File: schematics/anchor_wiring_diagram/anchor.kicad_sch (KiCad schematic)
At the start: 98 parts, among them J2 Screw_Terminal_01x01, J3 Screw_Terminal_01x01, J4 Screw_Terminal_01x01, J5 IEC_60320_C14_Receptacle, M1 Crossflow_Fan, M15 Fan, M16 Fan, M2 Crossflow_Fan, M20 Motor_X0, M21 Motor_Y0, M22 Motor_X1, M23 Motor_Y1, M24 Motor_Z2, M25 Motor_Z1, M26 Motor_Z0, M27 Motor_CPAP_Flap, M28 Motor_E0, M3 Fan_4pin, M4 Fan_4pin, M5 Fan_4pin, M6 Fan_4pin, M7 Fan, M8 Fan, SW1 SW_SPST, SW2 SW_SPST, SW5 SW_DPST, SW6 SW_DPST, SW7 SW_DPST, SW8 SW_DPST, T1 Meanwell UHP-200-5, T2 Meanwell UHP-200-48, T3 Meanwell UHP-200-24, U1 e-CAM20_CU0230, U12 Daylight_On_A_Stick_XXL, U13 Daylight_On_A_Stick_XXL, U16 Daylight_On_A_Stick_XXL, U17 Daylight_On_A_Stick_XXL, U2 OLED_HDMI_USB_Display, U20 Daylight_On_A_Stick_XXL, U21 Daylight_On_A_Stick_XXL, U24 Daylight_On_A_Stick_XXL, U25 Daylight_On_A_Stick_XXL, U26 5160T_Plus, U27 Adafruit_Feather_Relay, U29 Schneider_Electric_DPE25G7, U3 Overhub_7-Port_USB_3.0_MTT_Hub, U30 Crydom_D2440_SPST_SSR-NO, U31 Schneider_Electric_DPE25BL, U32 Neopixel_Strip, U33 Crydom_D2440_SPST_SSR-NO, U34 Schneider_Electric_DPE25BL, U37 Schneider_Electric_DPE25BL, U39 Raspberry_Pi, U4 Beacon_Regulator, U40 Beacon_Eddy_Scanner, U41 ThermEX26, U5 BTT_Octopus_Max_EZ, U6 5160T_Plus, U7 5160T_Plus, U8 5160T_Plus, U9 5160T_Plus

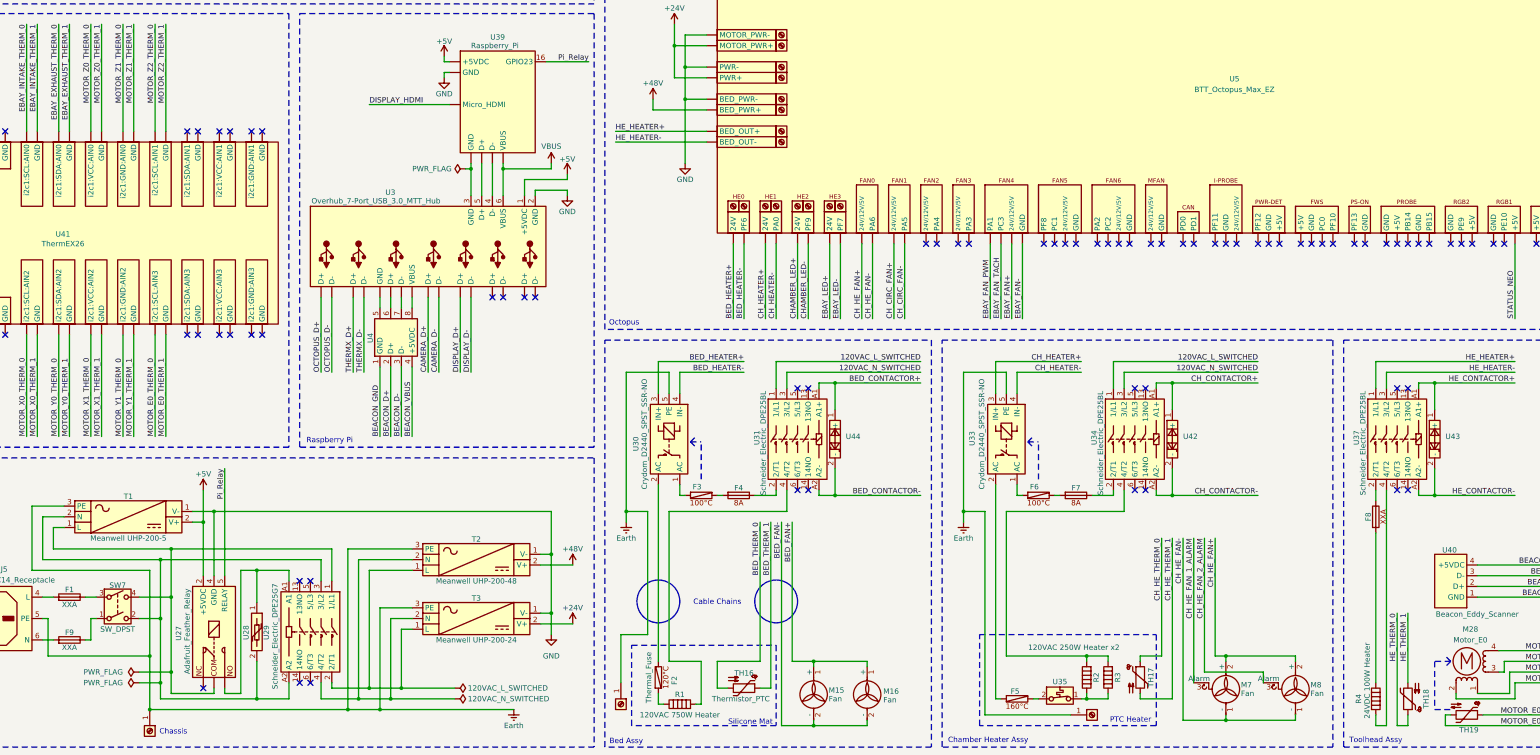
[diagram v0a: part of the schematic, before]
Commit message: schematic: wire up contactors
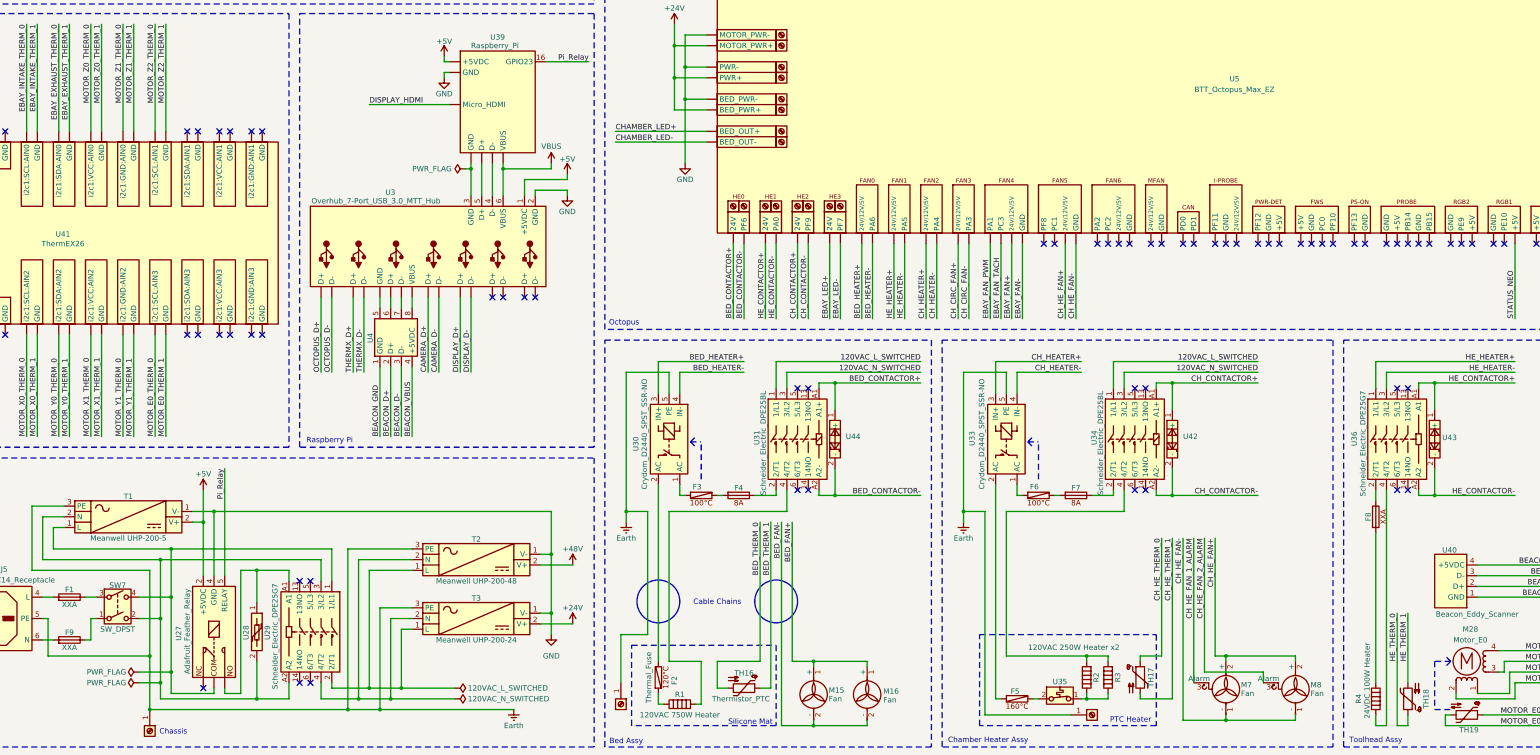
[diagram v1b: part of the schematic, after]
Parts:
- removed U37: Schneider_Electric_DPE25BL, symbol jmatt:Schneider_Electric_DPE25BL
- added U36: Schneider_Electric_DPE25G7, symbol jmatt:Schneider_Electric_DPE25G7
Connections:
- net +48V: no longer U5. (GND)
- net BED_CONTACTOR+: now also U5. (GND)
- net BED_CONTACTOR-: now also U5. (GND)
- net CH_CONTACTOR+: now also U5. (GND)
- net CH_CONTACTOR-: now also U5. (GND)
- net HE_CONTACTOR+: now also U5. (GND), U36.A1
- net HE_CONTACTOR-: now also U5. (GND), U36.A2
- net HE_HEATER+: now also U36.1 (1/L1)
- net HE_HEATER-: now also U36.3 (3/L2)
- net at F8.1: now also U36.2 (2/T1)
- net at U27.: now also U28.1, U29.A1
- net at R4.2: now also U36.4 (4/T2)
- new net: T2.1 (V-), T3.1 (V-), U29.2 (2/T1)
- new net: T2.2 (V+), T3.2 (V+), U29.4 (4/T2)
- no-connect marks 115 -> 109

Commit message: Add frame; k3z
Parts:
- added R5: 220R, symbol Device:R
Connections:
- net STATUS_NEO: now also R5.1; no longer SW8.1
- net at U27.: now also U28.1, U29.A1
- new net: R5.2, SW8.1
- new net: T2.1 (V-), T3.1 (V-), U29.2 (2/T1)
- new net: T2.2 (V+), T3.2 (V+), U29.4 (4/T2)
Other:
- moved on the sheet: SW8, U32
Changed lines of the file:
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@@
 	)
 	(junction
-		(at 64.77 96.52)
+		(at 72.39 96.52)
 		(diameter 0)
 		(color 255 0 0 1)
@@
 	)
 	(no_connect
+		(at 431.8 189.23)
+	)
+	(no_connect
 		(at 284.48 114.3)
 	)
@@
 	)
 	(no_connect
-		(at 100.33 96.52)
+		(at 107.95 96.52)
 	)
 	(no_connect
@@
 	)
 	(no_connect
-		(at 100.33 99.06)
+		(at 107.95 99.06)
 	)
 	(no_connect
@@
 	)
 	(no_connect
-		(at 100.33 101.6)
+		(at 107.95 101.6)
 	)
 	(no_connect
@@
 		(at 365.76 189.23)
 	)
-	(no_connect
-		(at 429.26 189.23)
-	)
 	(polyline
 		(pts
@@
 	(wire
 		(pts
-			(xy 44.45 96.52) (xy 52.07 96.52)
+			(xy 52.07 96.52) (xy 59.69 96.52)
 		)
 		(stroke
@@
 	(wire
 		(pts
+			(xy 429.26 189.23) (xy 429.26 207.01)
+		)
+		(stroke
+			(width 0)
+			(type default)
+		)
+	)
+	(wire
+		(pts
 			(xy 359.41 90.17) (xy 359.41 114.3)
 		)
@@
 	(wire
 		(pts
-			(xy 44.45 95.25) (xy 44.45 96.52)
+			(xy 52.07 95.25) (xy 52.07 96.52)
 		)
 		(stroke
@@
 	(wire
 		(pts
-			(xy 62.23 101.6) (xy 64.77 101.6)
+			(xy 69.85 101.6) (xy 72.39 101.6)
 		)
 		(stroke
@@
 	(wire
 		(pts
+			(xy 57.15 101.6) (xy 59.69 101.6)
+		)
+		(stroke
+			(width 0)
+			(type default)
+		)
+	)
+	(wire
+		(pts
 			(xy 38.1 76.2) (xy 52.07 76.2)
 		)
@@
 	(wire
 		(pts
-			(xy 64.77 99.06) (xy 67.31 99.06)
+			(xy 72.39 99.06) (xy 74.93 99.06)
 		)
 		(stroke
@@
 	(wire
 		(pts
+			(xy 38.1 101.6) (xy 49.53 101.6)
+		)
+		(stroke
+			(width 0)
+			(type default)
+		)
+	)
+	(wire
+		(pts
 			(xy 266.7 222.25) (xy 270.51 222.25)
 		)
@@
 	(wire
 		(pts
-			(xy 62.23 96.52) (xy 64.77 96.52)
+			(xy 69.85 96.52) (xy 72.39 96.52)
 		)
 		(stroke
@@
 	(wire
 		(pts
-			(xy 66.04 101.6) (xy 66.04 102.87)
+			(xy 73.66 101.6) (xy 73.66 102.87)
 		)
 		(stroke
@@
 	(wire
 		(pts
-			(xy 67.31 101.6) (xy 66.04 101.6)
+			(xy 74.93 101.6) (xy 73.66 101.6)
 		)
 		(stroke
@@
 	(wire
 		(pts
-			(xy 64.77 101.6) (xy 64.77 99.06)
+			(xy 72.39 101.6) (xy 72.39 99.06)
 		)
 		(stroke
@@
 	(wire
 		(pts
-			(xy 431.8 189.23) (xy 431.8 207.01)
-		)
-		(stroke
-			(width 0)
-			(type default)
-		)
-	)
-	(wire
-		(pts
 			(xy 354.33 22.86) (xy 356.87 22.86)
 		)
@@
 	(wire
 		(pts
-			(xy 64.77 95.25) (xy 64.77 96.52)
+			(xy 72.39 95.25) (xy 72.39 96.52)
 		)
 		(stroke
@@
 	(wire
 		(pts
-			(xy 64.77 96.52) (xy 67.31 96.52)
+			(xy 72.39 96.52) (xy 74.93 96.52)
 		)
 		(stroke
@@
 	(wire
 		(pts
-			(xy 38.1 101.6) (xy 52.07 101.6)
-		)
-		(stroke
-			(width 0)
-			(type default)
-		)
-	)
-	(wire
-		(pts
 			(xy 392.43 99.06) (xy 392.43 114.3)
 		)
@@
 	)
 	(label "STATUS_NEO"
-		(at 431.8 207.01 90)
+		(at 429.26 207.01 90)
 		(effects
 			(font
@@
 	)
 	(symbol
+		(lib_id "Device:R")
+		(at 53.34 101.6 90)
+		(unit 1)
+		(exclude_from_sim no)
+		(in_bom yes)
+		(on_board yes)
+		(dnp no)
+		(property "Reference" "R5"
+			(at 53.34 99.568 90)
+			(effects
+				(font
+					(size 1.27 1.27)
+				)
+			)
+		)
+		(property "Value" "220R"
+			(at 53.34 103.886 90)
+			(effects
+				(font
+					(size 1.27 1.27)
+				)
+			)
+		)
+		(property "Footprint" ""
+			(at 53.34 103.378 90)
+			(effects
+				(font
+					(size 1.27 1.27)
+				)
+				(hide yes)
+			)
+		)
+		(property "Datasheet" "~"
+			(at 53.34 101.6 0)
+			(effects
+				(font
+					(size 1.27 1.27)
+				)
+				(hide yes)
+			)
+		)
+		(property "Description" "Resistor"
+			(at 53.34 101.6 0)
+			(effects
+				(font
+					(size 1.27 1.27)
+				)
+				(hide yes)
+			)
+		)
+		(pin "1"
+		)
+		(pin "2"
+		)
+		(instances
+			(project ""
+				(path "/bf3f85ac-1500-41dc-b3d7-49dc05762e81"
+					(reference "R5")
+					(unit 1)
+				)
+			)
+		)
+	)
+	(symbol
 		(lib_id "Device:Heater")
 		(at 330.2 292.1 180)
@@
 	(symbol
 		(lib_id "power:GND")
-		(at 66.04 102.87 0)
+		(at 73.66 102.87 0)
 		(mirror y)
 		(unit 1)
@@
 		(dnp no)
 		(property "Reference" "#PWR0139"
-			(at 66.04 109.22 0)
+			(at 73.66 109.22 0)
 			(effects
 				(font
@@
 		)
 		(property "Value" "GND"
-			(at 66.04 106.68 0)
+			(at 73.66 106.68 0)
 			(effects
 				(font
@@
 		)
 		(property "Footprint" ""
-			(at 66.04 102.87 0)
+			(at 73.66 102.87 0)
 			(effects
 				(font
@@
 		)
 		(property "Datasheet" ""
-			(at 66.04 102.87 0)
+			(at 73.66 102.87 0)
 			(effects
 				(font
@@
 		)
 		(property "Description" "Power symbol creates a global label with name \"GND\" , ground"
-			(at 66.04 102.87 0)
+			(at 73.66 102.87 0)
 			(effects
 				(font
@@
 	(symbol
 		(lib_id "power:+5V")
-		(at 44.45 95.25 0)
+		(at 52.07 95.25 0)
 		(unit 1)
 		(exclude_from_sim no)
@@
 		(dnp no)
 		(property "Reference" "#PWR0133"
-			(at 44.45 99.06 0)
+			(at 52.07 99.06 0)
 			(effects
 				(font
@@
 		)
 		(property "Value" "+5V"
-			(at 44.45 91.694 0)
+			(at 52.07 91.694 0)
 			(effects
 				(font
@@
 		)
 		(property "Footprint" ""
-			(at 44.45 95.25 0)
+			(at 52.07 95.25 0)
 			(effects
 				(font
@@
 		)
 		(property "Datasheet" ""
-			(at 44.45 95.25 0)
+			(at 52.07 95.25 0)
 			(effects
 				(font
@@
 		)
 		(property "Description" "Power symbol creates a global label with name \"+5V\""
-			(at 44.45 95.25 0)
+			(at 52.07 95.25 0)
 			(effects
 				(font
@@
 	(symbol
 		(lib_id "Switch:SW_DPST")
-		(at 57.15 99.06 0)
+		(at 64.77 99.06 0)
 		(unit 1)
 		(exclude_from_sim no)
@@
 		(dnp no)
 		(property "Reference" "SW8"
-			(at 57.15 93.726 0)
+			(at 64.77 93.726 0)
 			(effects
 				(font
@@
 		)
 		(property "Value" "SW_DPST"
-			(at 57.15 104.14 0)
+			(at 64.77 104.14 0)
 			(effects
 				(font
@@
 		)
 		(property "Footprint" ""
-			(at 57.15 99.06 0)
+			(at 64.77 99.06 0)
 			(effects
 				(font
@@
 		)
 		(property "Datasheet" "~"
-			(at 57.15 99.06 0)
+			(at 64.77 99.06 0)
 			(effects
 				(font
@@
 		)
 		(property "Description" "Double Pole Single Throw (DPST) Switch"
-			(at 57.15 99.06 0)
+			(at 64.77 99.06 0)
 			(effects
 				(font
@@
 	(symbol
 		(lib_id "jmatt:Neopixel_Strip")
-		(at 83.82 93.98 0)
+		(at 91.44 93.98 0)
 		(unit 1)
 		(exclude_from_sim no)
@@
 		(dnp no)
 		(property "Reference" "U32"
-			(at 83.82 93.98 0)
+			(at 91.44 93.98 0)
 			(effects
 				(font
@@
 		)
 		(property "Value" "Neopixel_Strip"
-			(at 83.82 104.394 0)
+			(at 91.44 104.394 0)
 			(effects
 				(font
@@
 		)
 		(property "Footprint" ""
-			(at 83.82 93.98 0)
+			(at 91.44 93.98 0)
 			(effects
 				(font
@@
 		)
 		(property "Datasheet" ""
-			(at 83.82 93.98 0)
+			(at 91.44 93.98 0)
 			(effects
 				(font
@@
 		)
 		(property "Description" ""
-			(at 83.82 93.98 0)
+			(at 91.44 93.98 0)
 			(effects
 				(font
@@
 	(symbol
 		(lib_id "power:PWR_FLAG")
-		(at 64.77 95.25 0)
+		(at 72.39 95.25 0)
 		(unit 1)
 		(exclude_from_sim no)
@@
 		(dnp no)
 		(property "Reference" "#FLG07"
-			(at 64.77 93.345 0)
+			(at 72.39 93.345 0)
 			(effects
 				(font
@@
 		)
 		(property "Value" "PWR_FLAG"
-			(at 64.77 91.44 0)
+			(at 72.39 91.44 0)
 			(effects
 				(font
@@
 		)
 		(property "Footprint" ""
-			(at 64.77 95.25 0)
+			(at 72.39 95.25 0)
 			(effects
 				(font
@@
 		)
 		(property "Datasheet" "~"
-			(at 64.77 95.25 0)
+			(at 72.39 95.25 0)
 			(effects
 				(font
@@
 		)
 		(property "Description" "Special symbol for telling ERC where power comes from"
-			(at 64.77 95.25 0)
+			(at 72.39 95.25 0)
 			(effects
 				(font
